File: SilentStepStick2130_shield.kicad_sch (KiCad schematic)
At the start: 17 parts, among them J1 Conn_01x04_Socket, J2 Conn_01x04_Socket, J5 Conn_01x03, U1 TMC2130_SILENTSTEPSTICK, U2 TMC2130_SILENTSTEPSTICK

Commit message: v0
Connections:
- net +5V: no longer C1.1, C2.1, J5.2 (Pin_2), U1.9 (VM), U2.9 (VM)
- net DIR_1: now also IOL1.8 (Pin_8); no longer IOL1.6 (Pin_6)
- net DIR_2: now also IOL1.7 (Pin_7); no longer IOL1.5 (Pin_5)
- net IO2: now also U2.8 (~{EN}); no longer U2.2 (STEP)
- net IO3: now also U1.8 (~{EN}); no longer U1.2 (STEP)
- net OA1_1: now also J1.2 (Pin_2); no longer J1.3 (Pin_3)
- net OA1_2: now also J2.2 (Pin_2); no longer J2.3 (Pin_3)
- net OA2_1: now also J1.1 (Pin_1); no longer J1.4 (Pin_4)
- net OA2_2: now also J2.1 (Pin_1); no longer J2.4 (Pin_4)
- net OB1_1: now also J1.3 (Pin_3); no longer J1.2 (Pin_2)
- net OB1_2: now also J2.3 (Pin_3); no longer J2.2 (Pin_2)
- net OB2_1: now also J1.4 (Pin_4); no longer J1.1 (Pin_1)
- net OB2_2: now also J2.4 (Pin_4); no longer J2.1 (Pin_1)
- removed net IO6: IOL1.7 (Pin_7), U2.8 (~{EN})
- removed net IO7: IOL1.8 (Pin_8), U1.8 (~{EN})
- new net IO4: IOL1.5 (Pin_5), U2.2 (STEP)
- new net IO5: IOL1.6 (Pin_6), U1.2 (STEP)
- new net VM: C1.1, C2.1, J5.2 (Pin_2), U1.9 (VM), U2.9 (VM)
- no-connect marks 23 -> 24

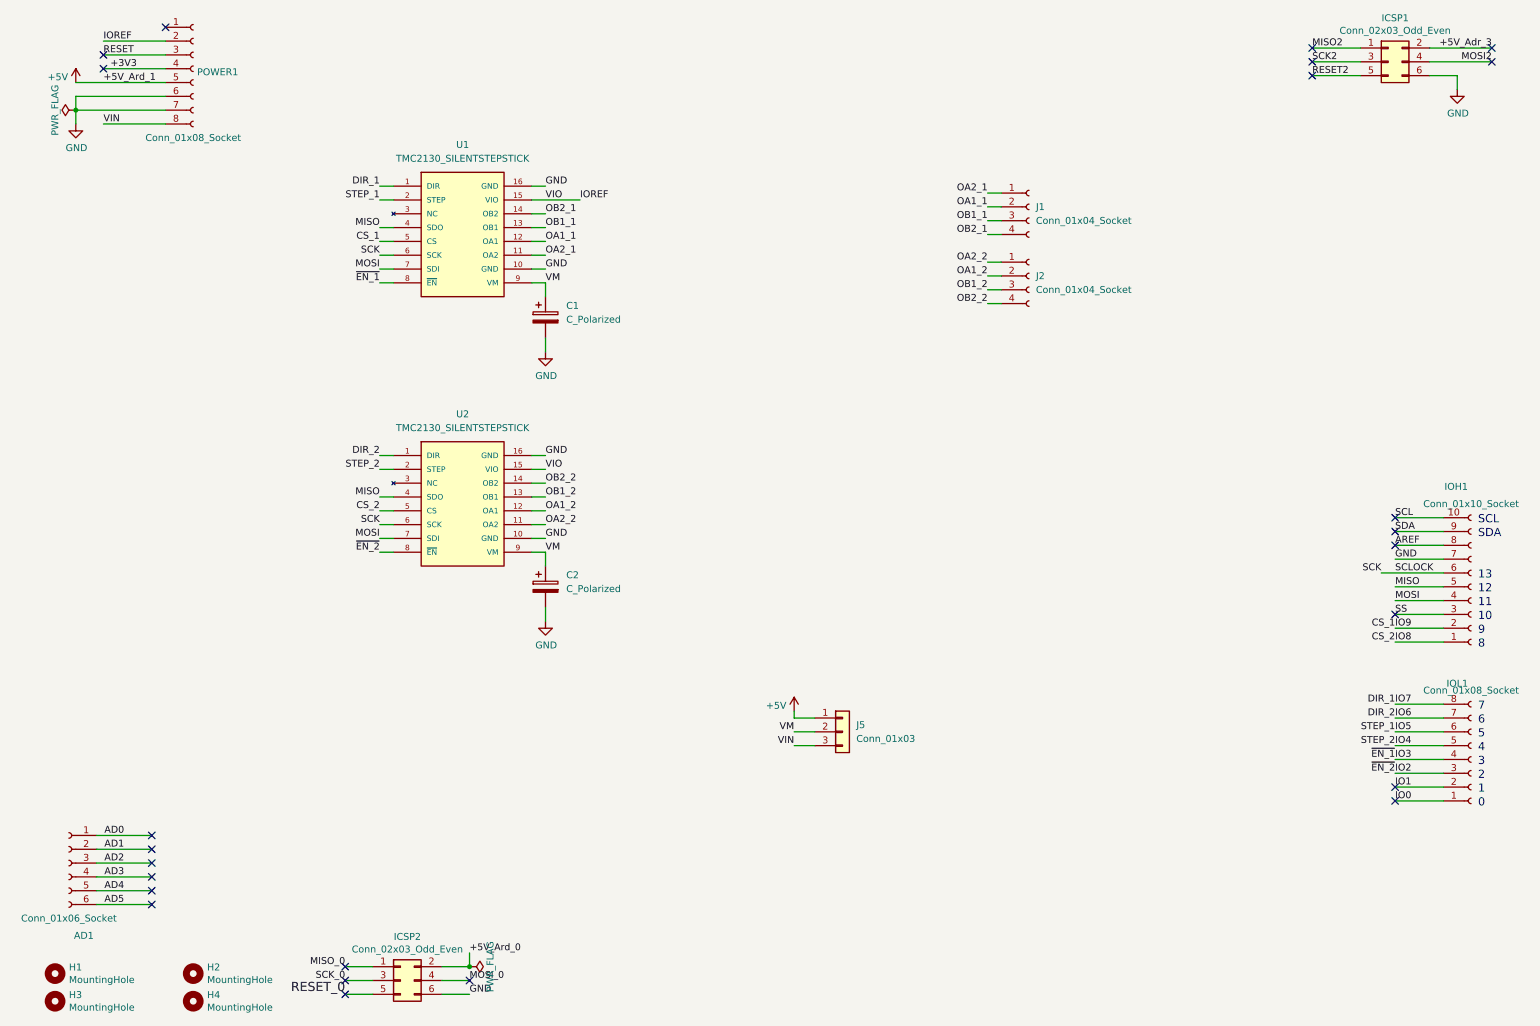
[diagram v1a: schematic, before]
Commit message: Changed to the new arduino symbol and moved the chipSelect from 11 12 to 12 13 Hard set enables to GND to get 3 digital input free for endcourse contacts Fliped the TMC2130 so that their backside faced up (changed the footprint)
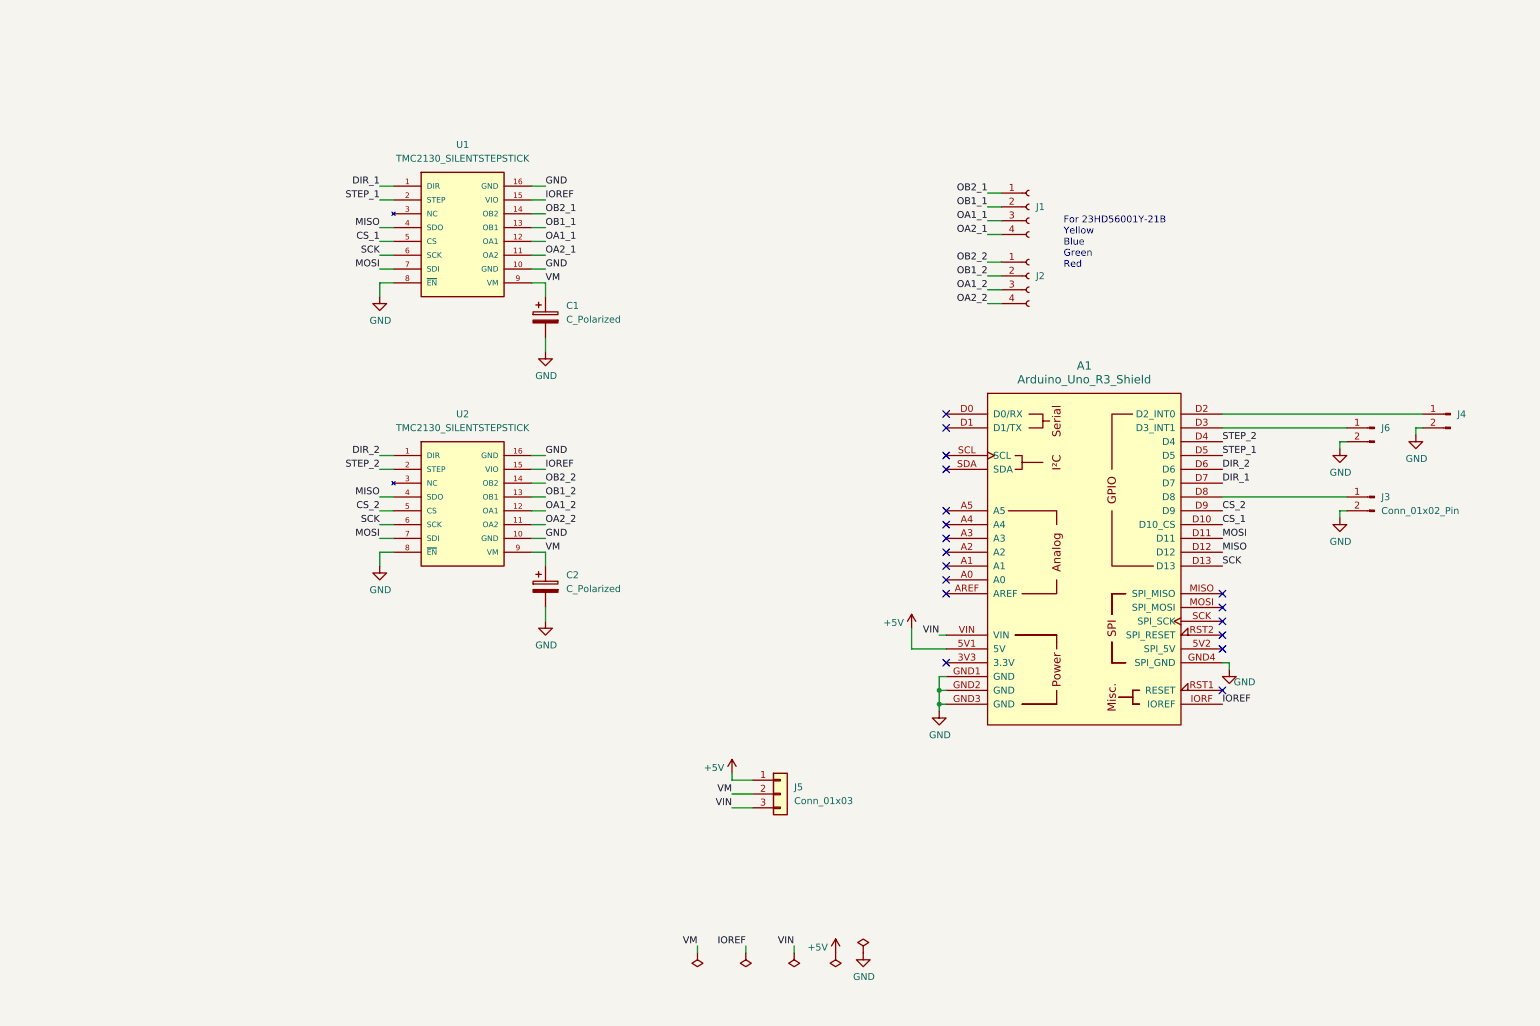
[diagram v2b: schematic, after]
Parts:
- removed AD1: Conn_01x06_Socket, Connector_PinHeader_2.54mm:PinHeader_1x06_P2.54mm_Vertical, symbol Connector:Conn_01x06_Socket
- removed H1, H2, H3, H4: MountingHole, MountingHole:MountingHole_3mm, symbol Mechanical:MountingHole
- removed ICSP1, ICSP2: Conn_02x03_Odd_Even, Connector_PinSocket_2.54mm:PinSocket_2x03_P2.54mm_Vertical, symbol Connector_Generic:Conn_02x03_Odd_Even
- removed IOH1: Conn_01x10_Socket, Connector_PinHeader_2.54mm:PinHeader_1x10_P2.54mm_Vertical, symbol Connector:Conn_01x10_Socket
- removed IOL1, POWER1: Conn_01x08_Socket, Connector_PinHeader_2.54mm:PinHeader_1x08_P2.54mm_Vertical, symbol Connector:Conn_01x08_Socket
- added A1: Arduino_Uno_R3_Shield, LibPersoNadj:Arduino_Uno_R3_Shield, symbol PCM_arduino-library:Arduino_Uno_R3_Shield
- added J3, J4, J6: Conn_01x02_Pin, Connector_JST:JST_PH_S2B-PH-K_1x02_P2.00mm_Horizontal, symbol Connector:Conn_01x02_Pin
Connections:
- net IO2 is gone; now on net GND: U2.8 (~{EN})
- net IO3 is gone; now on net GND: U1.8 (~{EN})
- net +5V: now also A1.5V1 (5V)
- net CS_1: now also A1.D10 (D10_CS)
- net CS_2: now also A1.D9
- net DIR_1: now also A1.D7
- net DIR_2: now also A1.D6
- net GND: now also A1.GND1 (GND), A1.GND2 (GND), A1.GND3 (GND), A1.GND4 (SPI_GND), J3.2 (Pin_2), J4.2 (Pin_2), J6.2 (Pin_2)
- net IOREF: now also A1.IORF (IOREF)
- net MISO: now also A1.D12
- net MOSI: now also A1.D11
- net OA1_1: now also J1.3 (Pin_3); no longer J1.2 (Pin_2)
- net OA1_2: now also J2.3 (Pin_3); no longer J2.2 (Pin_2)
- net OA2_1: now also J1.4 (Pin_4); no longer J1.1 (Pin_1)
- net OA2_2: now also J2.4 (Pin_4); no longer J2.1 (Pin_1)
- net OB1_1: now also J1.2 (Pin_2); no longer J1.3 (Pin_3)
- net OB1_2: now also J2.2 (Pin_2); no longer J2.3 (Pin_3)
- net OB2_1: now also J1.1 (Pin_1); no longer J1.4 (Pin_4)
- net OB2_2: now also J2.1 (Pin_1); no longer J2.4 (Pin_4)
- net SCK: now also A1.D13
- net VIN: now also A1.VIN
- net IO4 renamed STEP_2
- net STEP_2: now also A1.D4
- net IO5 renamed STEP_1
- net STEP_1: now also A1.D5
- new net: A1.D2 (D2_INT0), J4.1 (Pin_1)
- new net: A1.D3 (D3_INT1), J6.1 (Pin_1)
- new net: A1.D8, J3.1 (Pin_1)
- no-connect marks 24 -> 18
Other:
- note added: "For 23HD56001Y-21B Yellow Blue Green Red"
- note removed: "0"
- note removed: "1"
- note removed: "10"
- note removed: "11"
- note removed: "12"
- note removed: "13"
- note removed: "2"
- note removed: "3"
- note removed: "4"
- note removed: "5"
- note removed: "6"
- note removed: "7"
- note removed: "8"
- note removed: "9"
- note removed: "SCL"
- note removed: "SDA"
- moved on the sheet: J5

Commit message: Changed connectors for end course
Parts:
- J3, J4, J6: footprint Connector_JST:JST_PH_S2B-PH-K_1x02_P2.00mm_Horizontal -> Connector_JST:JST_XA_S02B-XASK-1_1x02_P2.50mm_Horizontal
- J5: symbol PCM_4ms_Connector:Conn_01x03 -> Connector:Conn_01x03_Socket
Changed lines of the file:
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@@
 (kicad_sch
-	(version 20231120)
+	(version 20250114)
 	(generator "eeschema")
-	(generator_version "8.0")
+	(generator_version "9.0")
 	(paper "A4")
+	(text "For 23HD56001Y-21B\nYellow\nBlue\nGreen\nRed"
+		(exclude_from_sim no)
+		(at 201.93 56.134 0)
+		(effects
+			(font
+				(size 1.27 1.27)
+			)
+			(justify left)
+		)
+	)
 	(junction
 		(at 179.07 140.97)
@@
 		)
 	)
-	(text "For 23HD56001Y-21B\nYellow\nBlue\nGreen\nRed"
-		(exclude_from_sim no)
-		(at 201.93 56.134 0)
-		(effects
-			(font
-				(size 1.27 1.27)
-			)
-			(justify left)
-		)
-	)
 	(label "OA2_1"
 		(at 187.96 54.61 180)
-		(fields_autoplaced yes)
 		(effects
 			(font
@@
 	(label "OA1_1"
 		(at 106.68 55.88 0)
-		(fields_autoplaced yes)
 		(effects
 			(font
@@
 	(label "STEP_1"
 		(at 76.2 48.26 180)
-		(fields_autoplaced yes)
 		(effects
 			(font
@@
 	(label "MISO"
 		(at 76.2 53.34 180)
-		(fields_autoplaced yes)
 		(effects
 			(font
@@
 	(label "MOSI"
 		(at 231.14 110.49 0)
-		(fields_autoplaced yes)
 		(effects
 			(font
@@
 	(label "DIR_1"
 		(at 231.14 100.33 0)
-		(fields_autoplaced yes)
 		(effects
 			(font
@@
 	(label "GND"
 		(at 106.68 110.49 0)
-		(fields_autoplaced yes)
 		(effects
 			(font
@@
 	(label "VM"
 		(at 140.97 157.48 180)
-		(fields_autoplaced yes)
 		(effects
 			(font
@@
 	(label "VM"
 		(at 106.68 113.03 0)
-		(fields_autoplaced yes)
 		(effects
 			(font
@@
 	(label "VM"
 		(at 106.68 63.5 0)
-		(fields_autoplaced yes)
 		(effects
 			(font
@@
 	(label "VIN"
 		(at 179.07 128.27 180)
-		(fields_autoplaced yes)
 		(effects
 			(font
@@
 	(label "IOREF"
 		(at 106.68 48.26 0)
-		(fields_autoplaced yes)
 		(effects
 			(font
@@
 	(label "OA2_1"
 		(at 106.68 58.42 0)
-		(fields_autoplaced yes)
 		(effects
 			(font
@@
 	(label "OB1_2"
 		(at 106.68 102.87 0)
-		(fields_autoplaced yes)
 		(effects
 			(font
@@
 	(label "OA1_1"
 		(at 187.96 52.07 180)
-		(fields_autoplaced yes)
 		(effects
 			(font
@@
 	(label "MOSI"
 		(at 76.2 60.96 180)
-		(fields_autoplaced yes)
 		(effects
 			(font
@@
 	(label "DIR_2"
 		(at 231.14 97.79 0)
-		(fields_autoplaced yes)
 		(effects
 			(font
@@
 	(label "OA2_2"
 		(at 106.68 107.95 0)
-		(fields_autoplaced yes)
 		(effects
 			(font
@@
 	(label "MISO"
 		(at 76.2 102.87 180)
-		(fields_autoplaced yes)
 		(effects
 			(font
@@
 	(label "OA2_2"
 		(at 187.96 67.31 180)
-		(fields_autoplaced yes)
 		(effects
 			(font
@@
 	(label "OB1_1"
 		(at 106.68 53.34 0)
-		(fields_autoplaced yes)
 		(effects
 			(font
@@
 	(label "CS_2"
 		(at 231.14 105.41 0)
-		(fields_autoplaced yes)
 		(effects
 			(font
@@
 	(label "SCK"
 		(at 76.2 107.95 180)
-		(fields_autoplaced yes)
 		(effects
 			(font
@@
 	(label "DIR_1"
 		(at 76.2 45.72 180)
-		(fields_autoplaced yes)
 		(effects
 			(font
@@
 	(label "MOSI"
 		(at 76.2 110.49 180)
-		(fields_autoplaced yes)
 		(effects
 			(font
@@
 	(label "VM"
 		(at 134.62 185.42 180)
-		(fields_autoplaced yes)
 		(effects
 			(font
@@
 	(label "CS_2"
 		(at 76.2 105.41 180)
-		(fields_autoplaced yes)
 		(effects
 			(font
@@
 	(label "IOREF"
 		(at 231.14 140.97 0)
-		(fields_autoplaced yes)
 		(effects
 			(font
@@
 	(label "VIN"
 		(at 140.97 160.02 180)
-		(fields_autoplaced yes)
 		(effects
 			(font
@@
 	(label "SCK"
 		(at 76.2 58.42 180)
-		(fields_autoplaced yes)
 		(effects
 			(font
@@
 	(label "OB2_1"
 		(at 106.68 50.8 0)
-		(fields_autoplaced yes)
 		(effects
 			(font
@@
 	(label "STEP_1"
 		(at 231.14 95.25 0)
-		(fields_autoplaced yes)
 		(effects
 			(font
@@
 	(label "STEP_2"
 		(at 76.2 97.79 180)
-		(fields_autoplaced yes)
 		(effects
 			(font
@@
 	(label "IOREF"
 		(at 143.51 185.42 180)
-		(fields_autoplaced yes)
 		(effects
 			(font
@@
 	(label "OB2_2"
 		(at 106.68 100.33 0)
-		(fields_autoplaced yes)
 		(effects
 			(font
@@
 	(label "OB1_2"
 		(at 187.96 62.23 180)
-		(fields_autoplaced yes)
 		(effects
 			(font
@@
 	(label "OB2_1"
 		(at 187.96 46.99 180)
-		(fields_autoplaced yes)
 		(effects
 			(font
@@
 	(label "OB2_2"
 		(at 187.96 59.69 180)
-		(fields_autoplaced yes)
 		(effects
 			(font
@@
 	(label "VIN"
 		(at 152.4 185.42 180)
-		(fields_autoplaced yes)
 		(effects
 			(font
@@
 	(label "GND"
 		(at 106.68 45.72 0)
-		(fields_autoplaced yes)
 		(effects
 			(font
@@
 	(label "MISO"
 		(at 231.14 113.03 0)
-		(fields_autoplaced yes)
 		(effects
 			(font
@@
 	(label "GND"
 		(at 106.68 60.96 0)
-		(fields_autoplaced yes)
 		(effects
 			(font
@@
 	(label "SCK"
 		(at 231.14 115.57 0)
-		(fields_autoplaced yes)
 		(effects
 			(font
@@
 	(label "OA1_2"
 		(at 106.68 105.41 0)
-		(fields_autoplaced yes)
 		(effects
 			(font
@@
 	(label "OB1_1"
 		(at 187.96 49.53 180)
-		(fields_autoplaced yes)
 		(effects
 			(font
@@
 	(label "IOREF"
 		(at 106.68 97.79 0)
-		(fields_autoplaced yes)
 		(effects
 			(font
@@
 	(label "DIR_2"
 		(at 76.2 95.25 180)
-		(fields_autoplaced yes)
 		(effects
 			(font
@@
 	(label "GND"
 		(at 106.68 95.25 0)
-		(fields_autoplaced yes)
 		(effects
 			(font
@@
 	(label "CS_1"
 		(at 76.2 55.88 180)
-		(fields_autoplaced yes)
 		(effects
 			(font
@@
 	(label "CS_1"
 		(at 231.14 107.95 0)
-		(fields_autoplaced yes)
 		(effects
 			(font
@@
 	(label "OA1_2"
 		(at 187.96 64.77 180)
-		(fields_autoplaced yes)
 		(effects
 			(font
@@
 	(label "STEP_2"
 		(at 231.14 92.71 0)
-		(fields_autoplaced yes)
 		(effects
 			(font
@@
 			)
 		)
-		(property "Footprint" "Connector_JST:JST_PH_S2B-PH-K_1x02_P2.00mm_Horizontal"
+		(property "Footprint" "Connector_JST:JST_XA_S02B-XASK-1_1x02_P2.50mm_Horizontal"
 			(at 273.05 87.63 0)
 			(effects
@@
 			)
 		)
-		(property "Footprint" "Connector_JST:JST_PH_S2B-PH-K_1x02_P2.00mm_Horizontal"
+		(property "Footprint" "Connector_JST:JST_XA_S02B-XASK-1_1x02_P2.50mm_Horizontal"
 			(at 259.08 90.17 0)
 			(effects
@@
 	)
 	(symbol
-		(lib_id "PCM_4ms_Connector:Conn_01x03")
+		(lib_id "Connector:Conn_01x03_Socket")
 		(at 149.86 157.48 0)
 		(unit 1)
@@
 		(fields_autoplaced yes)
 		(property "Reference" "J5"
-			(at 152.4 156.2099 0)
+			(at 151.13 156.2099 0)
 			(effects
 				(font
@@
 		)
 		(property "Value" "Conn_01x03"
-			(at 152.4 158.7499 0)
+			(at 151.13 158.7499 0)
 			(effects
 				(font
@@
 		)
 		(property "Footprint" "Connector_PinHeader_2.54mm:PinHeader_1x03_P2.54mm_Vertical"
-			(at 149.86 150.495 0)
+			(at 149.86 157.48 0)
 			(effects
 				(font
@@
 			)
 		)
-		(property "Datasheet" ""
+		(property "Datasheet" "~"
 			(at 149.86 157.48 0)
 			(effects
@@
 			)
 		)
-		(property "Description" "HEADER 1x3 MALE PINS 0.100” 180deg"
+		(property "Description" "Generic connector, single row, 01x03, script generated"
 			(at 149.86 157.48 0)
 			(effects
@@
 			)
 		)
-		(property "Footprint" "Connector_JST:JST_PH_S2B-PH-K_1x02_P2.00mm_Horizontal"
+		(property "Footprint" "Connector_JST:JST_XA_S02B-XASK-1_1x02_P2.50mm_Horizontal"
 			(at 259.08 102.87 0)
 			(effects
@@
 		)
 	)
+	(embedded_fonts no)
 )
